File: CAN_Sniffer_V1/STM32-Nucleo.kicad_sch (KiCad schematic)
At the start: 5 parts, among them U3 STM32F072CBTx, Y2 Crystal

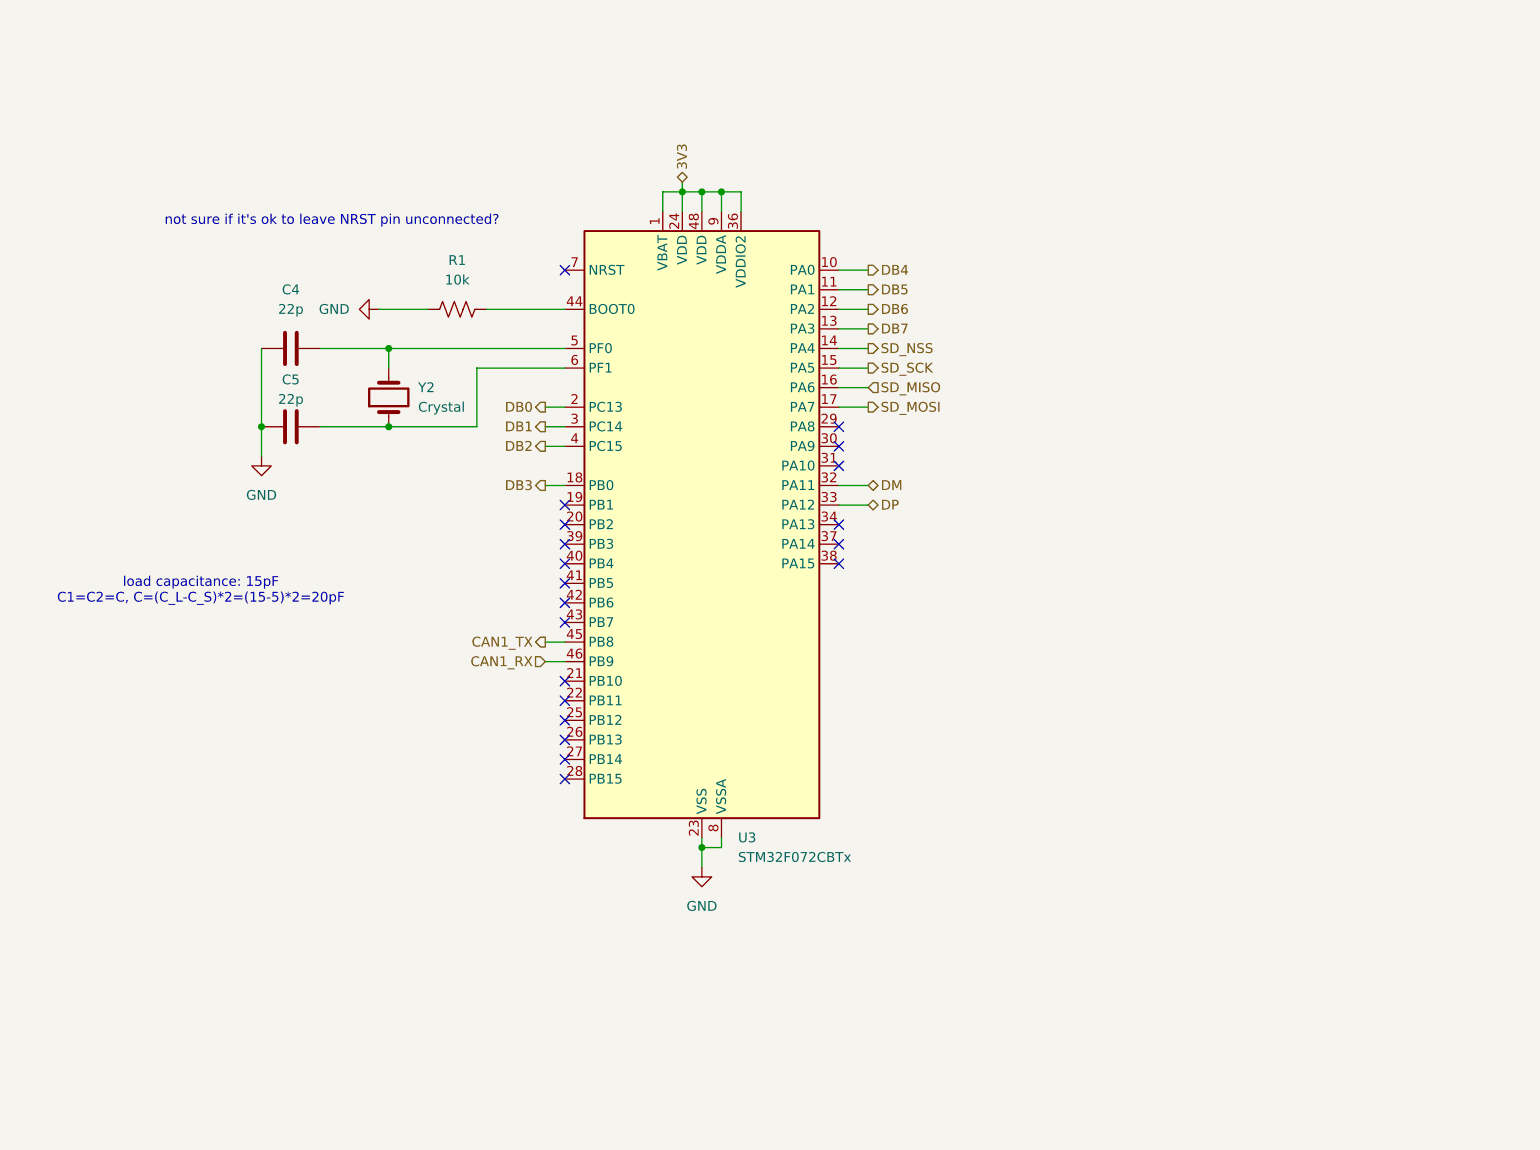
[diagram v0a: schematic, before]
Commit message: changed power schem, pinouts, first iteration layout
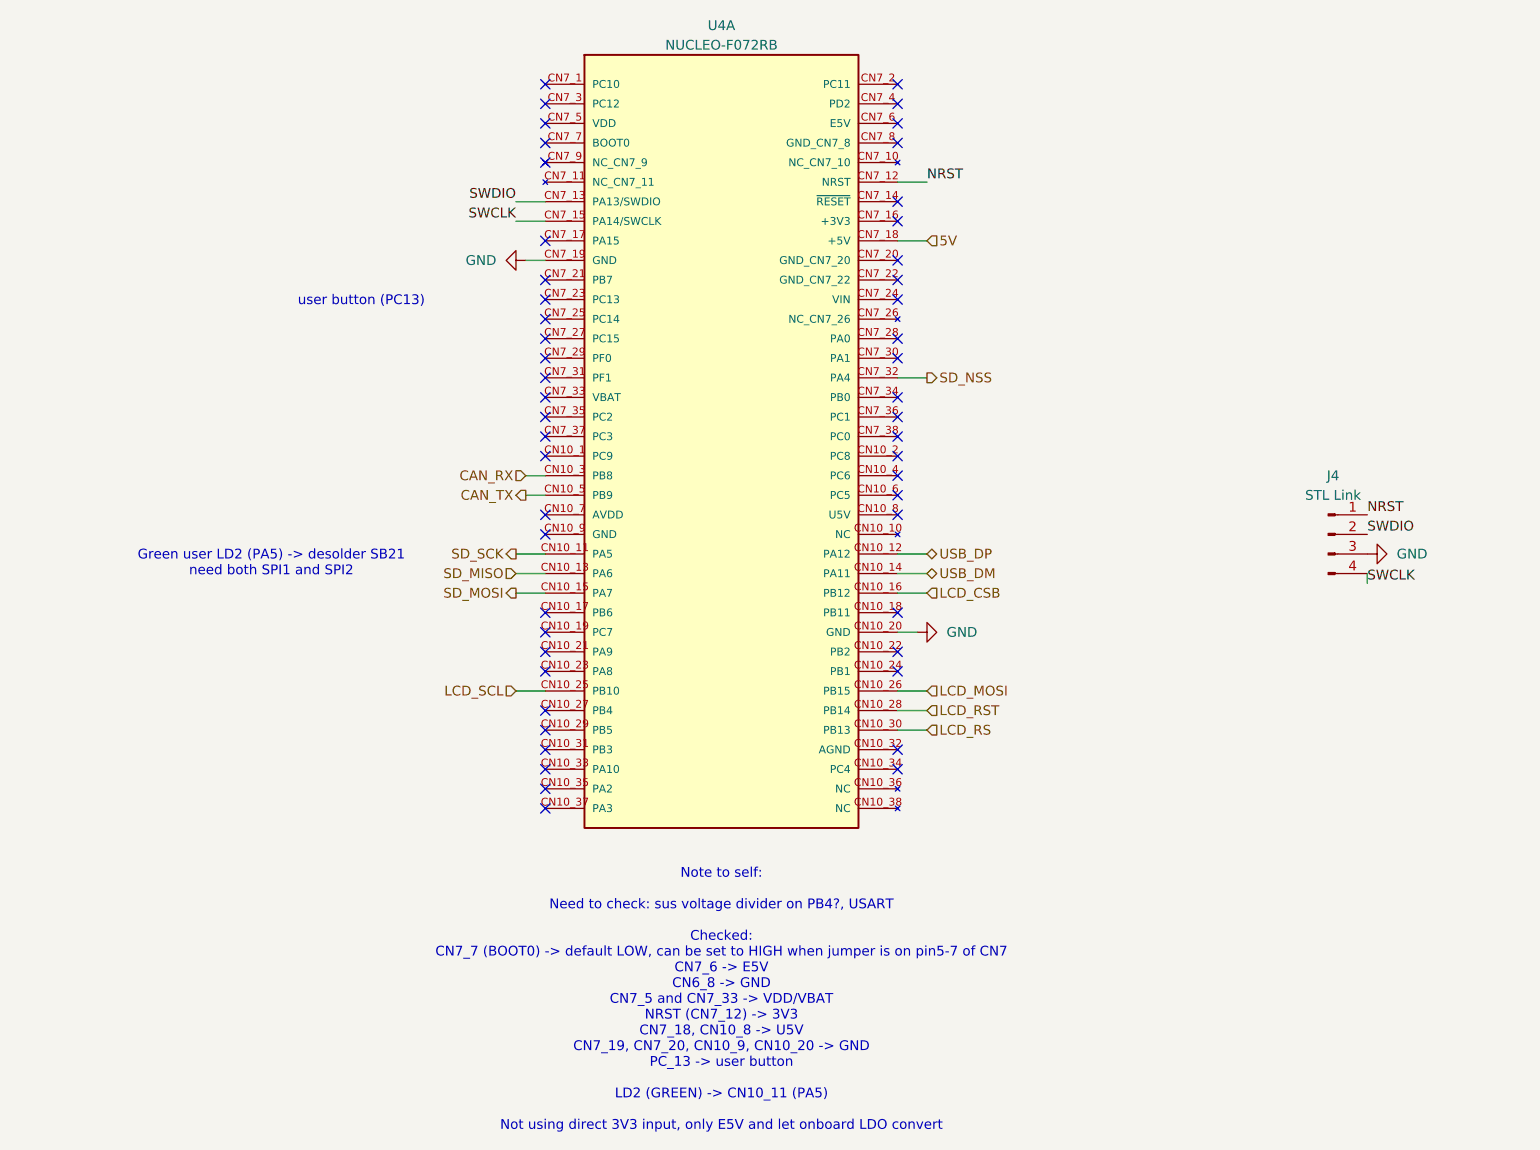
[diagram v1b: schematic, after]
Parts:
- removed C4, C5: 22p, Capacitor_SMD:C_0805_2012Metric_Pad1.18x1.45mm_HandSolder, symbol Device:C
- removed R1: 10k, Resistor_SMD:R_0805_2012Metric_Pad1.20x1.40mm_HandSolder, symbol Device:R_US
- removed U3: STM32F072CBTx, Package_QFP:LQFP-48_7x7mm_P0.5mm, symbol MCU_ST_STM32F0:STM32F072CBTx
- removed Y2: Crystal, Mouser_Parts:AbraconASD, symbol Device:Crystal
- added J4: STL Link, Connector_PinHeader_2.54mm:PinHeader_1x04_P2.54mm_Vertical, symbol Connector:Conn_01x04_Pin
- added U4: NUCLEO-F072RB, STM32F0_breakout:MODULE_NUCLEO-F072RB, symbol NUCLEO-F072RB:NUCLEO-F072RB
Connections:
- net GND: now also J4.3 (Pin_3), U4.CN10_20 (GND), U4.CN7_19 (GND)
- net SD_MISO: now also U4.CN10_13 (PA6)
- net SD_MOSI: now also U4.CN10_15 (PA7)
- net SD_NSS: now also U4.CN7_32 (PA4)
- net SD_SCK: now also U4.CN10_11 (PA5)
- new net 5V: U4.CN7_18 (+5V)
- new net CAN_RX: U4.CN10_3 (PB8)
- new net CAN_TX: U4.CN10_5 (PB9)
- new net LCD_CSB: U4.CN10_16 (PB12)
- new net LCD_MOSI: U4.CN10_26 (PB15)
- new net LCD_RS: U4.CN10_30 (PB13)
- new net LCD_RST: U4.CN10_28 (PB14)
- new net LCD_SCL: U4.CN10_25 (PB10)
- new net NRST: J4.1 (Pin_1), U4.CN7_12 (NRST)
- new net SWCLK: J4.4 (Pin_4), U4.CN7_15 (PA14/SWCLK)
- new net SWDIO: J4.2 (Pin_2), U4.CN7_13 (PA13/SWDIO)
- new net USB_DM: U4.CN10_14 (PA11)
- new net USB_DP: U4.CN10_12 (PA12)
- no-connect marks 20 -> 51
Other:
- note added: "Green user LD2 (PA5) -> desolder SB21 need both SPI1 and SPI2"
- note added: "Note to self: Need to check: sus voltage divider on PB4?, USART Checked: CN7_7 (BOOT0) -> default LOW, can be set to HIGH when jumper is on pin5-7 of CN7 CN7_6 -> E5V CN6_8 -> GND CN7_5 and CN7_33 -> VDD/VBAT NRST (CN7_12) -> 3V3 CN7_18, CN10_8 -> U5V CN7_19, CN7_20, CN10_9, CN10_20 -> GND PC_13 -> user button LD2 (GREEN) -> CN10_11 (PA5) Not using direct 3V3 input, only E5V and let onboard LDO c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"
- note added: "user button (PC13)"
- note removed: "load capacitance: 15pF C1=C2=C, C=(C_L-C_S)*2=(15-5)*2=20pF"
- note removed: "not sure if it's ok to leave NRST pin unconnected?"

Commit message: iteration 2 routing
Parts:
- removed J4: STL Link, Connector_PinHeader_2.54mm:PinHeader_1x04_P2.54mm_Vertical, symbol Connector:Conn_01x04_Pin
- removed U4: NUCLEO-F072RB, STM32F0_breakout:MODULE_NUCLEO-F072RB, symbol NUCLEO-F072RB:NUCLEO-F072RB
- added C6: 100n, Capacitor_SMD:C_0805_2012Metric_Pad1.18x1.45mm_HandSolder, symbol bfr_capacitors:08051C104KAT4A
- added J1: Conn_01x02_Socket, Connector_PinHeader_2.54mm:PinHeader_1x02_P2.54mm_Vertical, symbol Connector:Conn_01x02_Socket
- added U3: NUCLEO-F072RB, STM32F0_breakout:MODULE_NUCLEO-F072RB, symbol NUCLEO-F072RB:NUCLEO-F072RB
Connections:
- net 5V: now also U3.CN7_18 (+5V)
- net CAN_RX: now also U3.CN10_3 (PB8)
- net CAN_TX: now also U3.CN10_5 (PB9)
- net GND: now also C6.2, U3.CN10_20 (GND_CN10_20), U3.CN7_19 (GND_CN7_19)
- net LCD_CSB: now also U3.CN10_16 (PB12)
- net LCD_MOSI: now also U3.CN10_26 (PB15)
- net LCD_RS: now also U3.CN10_30 (PB13)
- net LCD_RST: now also U3.CN10_28 (PB14)
- net LCD_SCL: now also U3.CN10_25 (PB10)
- net SD_MISO: now also U3.CN10_27 (PB4)
- net SD_MOSI: now also U3.CN10_29 (PB5)
- net SD_NSS: now also U3.CN7_17 (PA15)
- net SD_SCK: now also U3.CN10_31 (PB3)
- new net 3V3: U3.CN7_16 (+3V3)
- new net SD_CD: U3.CN10_33 (PA10)
- new net U5V: C6.1, J1.1 (Pin_1)
- no-connect marks 51 -> 54
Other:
- note added: "5V (input to nucleo as E5V) 3V3 (output from nucleo's LDO)"
- note added: "Green user LD2 (PA5)"
- note added: "jumper from U5V pin of nucleo"
- note removed: "Green user LD2 (PA5) -> desolder SB21 need both SPI1 and SPI2"
- note removed: "Note to self: Need to check: sus voltage divider on PB4?, USART Checked: CN7_7 (BOOT0) -> default LOW, can be set to HIGH when jumper is on pin5-7 of CN7 CN7_6 -> E5V CN6_8 -> GND CN7_5 and CN7_33 -> VDD/VBAT NRST (CN7_12) -> 3V3 CN7_18, CN10_8 -> U5V CN7_19, CN7_20, CN10_9, CN10_20 -> GND PC_13 -> user button LD2 (GREEN) -> CN10_11 (PA5) Not using direct 3V3 input, only E5V and let onboard LDO c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"

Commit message: sync changes
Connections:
- net GND: now also J1.2 (Pin_2)
- no-connect marks 54 -> 53
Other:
- moved on the sheet: C6
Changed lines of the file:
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@@
 	)
 	(junction
-		(at 69.85 129.54)
+		(at 77.47 138.43)
 		(diameter 0)
 		(color 0 0 0 0)
 	)
+	(junction
+		(at 77.47 129.54)
+		(diameter 0)
+		(color 0 0 0 0)
+	)
 	(no_connect
 		(at 154.94 77.47)
@@
 	)
 	(no_connect
-		(at 86.36 132.08)
-	)
-	(no_connect
 		(at 64.77 87.63)
 	)
@@
 	(wire
 		(pts
+			(xy 77.47 129.54) (xy 86.36 129.54)
+		)
+		(stroke
+			(width 0)
+			(type default)
+		)
+	)
+	(wire
+		(pts
 			(xy 200.66 92.71) (xy 204.47 92.71)
 		)
@@
 	(wire
 		(pts
+			(xy 86.36 138.43) (xy 77.47 138.43)
+		)
+		(stroke
+			(width 0)
+			(type default)
+		)
+	)
+	(wire
+		(pts
 			(xy 200.66 97.79) (xy 204.47 97.79)
 		)
@@
 	(wire
 		(pts
+			(xy 86.36 132.08) (xy 86.36 138.43)
+		)
+		(stroke
+			(width 0)
+			(type default)
+		)
+	)
+	(wire
+		(pts
 			(xy 152.4 67.31) (xy 154.94 67.31)
 		)
@@
 	(wire
 		(pts
-			(xy 69.85 137.16) (xy 69.85 138.43)
+			(xy 77.47 137.16) (xy 77.47 138.43)
 		)
 		(stroke
@@
 	(wire
 		(pts
-			(xy 67.31 129.54) (xy 69.85 129.54)
+			(xy 67.31 129.54) (xy 77.47 129.54)
 		)
 		(stroke
@@
 		(pts
 			(xy 151.13 100.33) (xy 154.94 100.33)
-		)
-		(stroke
-			(width 0)
-			(type default)
-		)
-	)
-	(wire
-		(pts
-			(xy 69.85 129.54) (xy 86.36 129.54)
 		)
 		(stroke
@@
 	(symbol
 		(lib_id "bfr_capacitors:08051C104KAT4A")
-		(at 69.85 133.35 0)
+		(at 77.47 133.35 0)
 		(unit 1)
 		(exclude_from_sim no)
@@
 		(fields_autoplaced yes)
 		(property "Reference" "C6"
-			(at 73.66 132.0799 0)
+			(at 81.28 132.0799 0)
 			(effects
 				(font
@@
 		)
 		(property "Value" "100n"
-			(at 73.66 134.6199 0)
+			(at 81.28 134.6199 0)
 			(effects
 				(font
@@
 		)
 		(property "Footprint" "Capacitor_SMD:C_0805_2012Metric_Pad1.18x1.45mm_HandSolder"
-			(at 69.85 135.89 0)
+			(at 77.47 135.89 0)
 			(effects
 				(font
@@
 		)
 		(property "Datasheet" ""
-			(at 69.85 137.16 0)
+			(at 77.47 137.16 0)
 			(effects
 				(font
@@
 		)
 		(property "Description" "100nF±10% X7R 25V JLCPCB Basic 0805 Capacitor"
-			(at 69.85 133.35 0)
+			(at 77.47 133.35 0)
 			(effects
 				(font
@@
 		)
 		(property "Sim.Device" "SUBCKT"
-			(at 69.85 138.43 0)
+			(at 77.47 138.43 0)
 			(effects
 				(font
@@
 		)
 		(property "Sim.Pins" "1=P1 2=P2"
-			(at 69.85 139.7 0)
+			(at 77.47 139.7 0)
 			(effects
 				(font
@@
 		)
 		(property "Sim.Name" "08051C104KAT4A"
-			(at 69.85 142.24 0)
+			(at 77.47 142.24 0)
 			(effects
 				(font
@@
 		)
 		(property "Pretty Name" "100nF 25V 0805 Capacitor"
-			(at 69.85 143.51 0)
+			(at 77.47 143.51 0)
 			(effects
 				(font
@@
 		)
 		(property "Qty/Unit" ""
-			(at 69.85 144.78 0)
+			(at 77.47 144.78 0)
 			(effects
 				(font
@@
 		)
 		(property "Cost/Unit" ""
-			(at 69.85 146.05 0)
+			(at 77.47 146.05 0)
 			(effects
 				(font
@@
 		)
 		(property "Order From" "LCSC"
-			(at 69.85 147.32 0)
+			(at 77.47 147.32 0)
 			(effects
 				(font
@@
 		)
 		(property "Digikey P/N" ""
-			(at 69.85 148.59 0)
+			(at 77.47 148.59 0)
 			(effects
 				(font
@@
 		)
 		(property "Mouser P/N" "581-08051C104KAT4A"
-			(at 69.85 148.59 0)
+			(at 77.47 148.59 0)
 			(effects
 				(font
@@
 		)
 		(property "LCSC P/N" "C28233"
-			(at 69.85 148.59 0)
+			(at 77.47 148.59 0)
 			(effects
 				(font
@@
 		)
 		(property "JLCPCB Basic Part" "Yes"
-			(at 69.85 148.59 0)
+			(at 77.47 148.59 0)
 			(effects
 				(font
@@
 		)
 		(property "Created by" "capacitor_generator.py script using capacitor_bible_spec.txt"
-			(at 69.85 148.59 0)
+			(at 77.47 148.59 0)
 			(effects
 				(font
@@
 		(on_board yes)
 		(dnp no)
-		(fields_autoplaced yes)
 		(property "Reference" "J1"
-			(at 90.805 137.16 0)
+			(at 104.14 132.08 0)
 			(effects
 				(font
@@
 		)
 		(property "Value" "Conn_01x02_Socket"
-			(at 90.805 134.62 0)
+			(at 104.14 129.54 0)
 			(effects
 				(font
@@
 	(symbol
 		(lib_id "power:GND")
-		(at 69.85 138.43 0)
+		(at 77.47 138.43 0)
 		(unit 1)
 		(exclude_from_sim no)
@@
 		(fields_autoplaced yes)
 		(property "Reference" "#PWR012"
-			(at 69.85 144.78 0)
+			(at 77.47 144.78 0)
 			(effects
 				(font
@@
 		)
 		(property "Value" "GND"
-			(at 69.85 143.51 0)
+			(at 77.47 143.51 0)
 			(effects
 				(font
@@
 		)
 		(property "Footprint" ""
-			(at 69.85 138.43 0)
+			(at 77.47 138.43 0)
 			(effects
 				(font
@@
 		)
 		(property "Datasheet" ""
-			(at 69.85 138.43 0)
+			(at 77.47 138.43 0)
 			(effects
 				(font
@@
 		)
 		(property "Description" "Power symbol creates a global label with name \"GND\" , ground"
-			(at 69.85 138.43 0)
-			(effects
-				(font
+			(at 77.47 138.43 0)
+			(effects
+				(font
